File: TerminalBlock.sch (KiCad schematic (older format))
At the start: 0 parts

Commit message: Refactoring and Created key shortcuts
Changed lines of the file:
@@
 $Descr A4 11693 8268
 encoding utf-8
-Sheet 9 9
+Sheet 8 9
 Title ""
-Date "9 feb 2014"
+Date "18 feb 2014"
 Rev ""
 Comp ""
@@
 L +3.3V #PWR?
 U 1 1 52F86033
-P 2850 1050
-F 0 "#PWR?" H 2850 1010 30  0001 C CNN
-F 1 "+3.3V" H 2850 1160 30  0000 C CNN
-F 2 "" H 2850 1050 60  0000 C CNN
-F 3 "" H 2850 1050 60  0000 C CNN
-	1    2850 1050
+P 2100 850
+F 0 "#PWR?" H 2100 810 30  0001 C CNN
+F 1 "+3.3V" H 2100 960 30  0000 C CNN
+F 2 "" H 2100 850 60  0000 C CNN
+F 3 "" H 2100 850 60  0000 C CNN
+	1    2100 850
 	1    0    0    -1
 $EndComp
@@
 L +5V #PWR?
 U 1 1 52F86042
-P 2850 1400
-F 0 "#PWR?" H 2850 1490 20  0001 C CNN
-F 1 "+5V" H 2850 1490 30  0000 C CNN
-F 2 "" H 2850 1400 60  0000 C CNN
-F 3 "" H 2850 1400 60  0000 C CNN
-	1    2850 1400
+P 2100 1200
+F 0 "#PWR?" H 2100 1290 20  0001 C CNN
+F 1 "+5V" H 2100 1290 30  0000 C CNN
+F 2 "" H 2100 1200 60  0000 C CNN
+F 3 "" H 2100 1200 60  0000 C CNN
+	1    2100 1200
 	1    0    0    -1
 $EndComp
@@
 L GND #PWR?
 U 1 1 52F86051
-P 2850 1750
-F 0 "#PWR?" H 2850 1750 30  0001 C CNN
-F 1 "GND" H 2850 1680 30  0001 C CNN
-F 2 "" H 2850 1750 60  0000 C CNN
-F 3 "" H 2850 1750 60  0000 C CNN
-	1    2850 1750
+P 2100 1550
+F 0 "#PWR?" H 2100 1550 30  0001 C CNN
+F 1 "GND" H 2100 1480 30  0001 C CNN
+F 2 "" H 2100 1550 60  0000 C CNN
+F 3 "" H 2100 1550 60  0000 C CNN
+	1    2100 1550
 	1    0    0    -1
 $EndComp

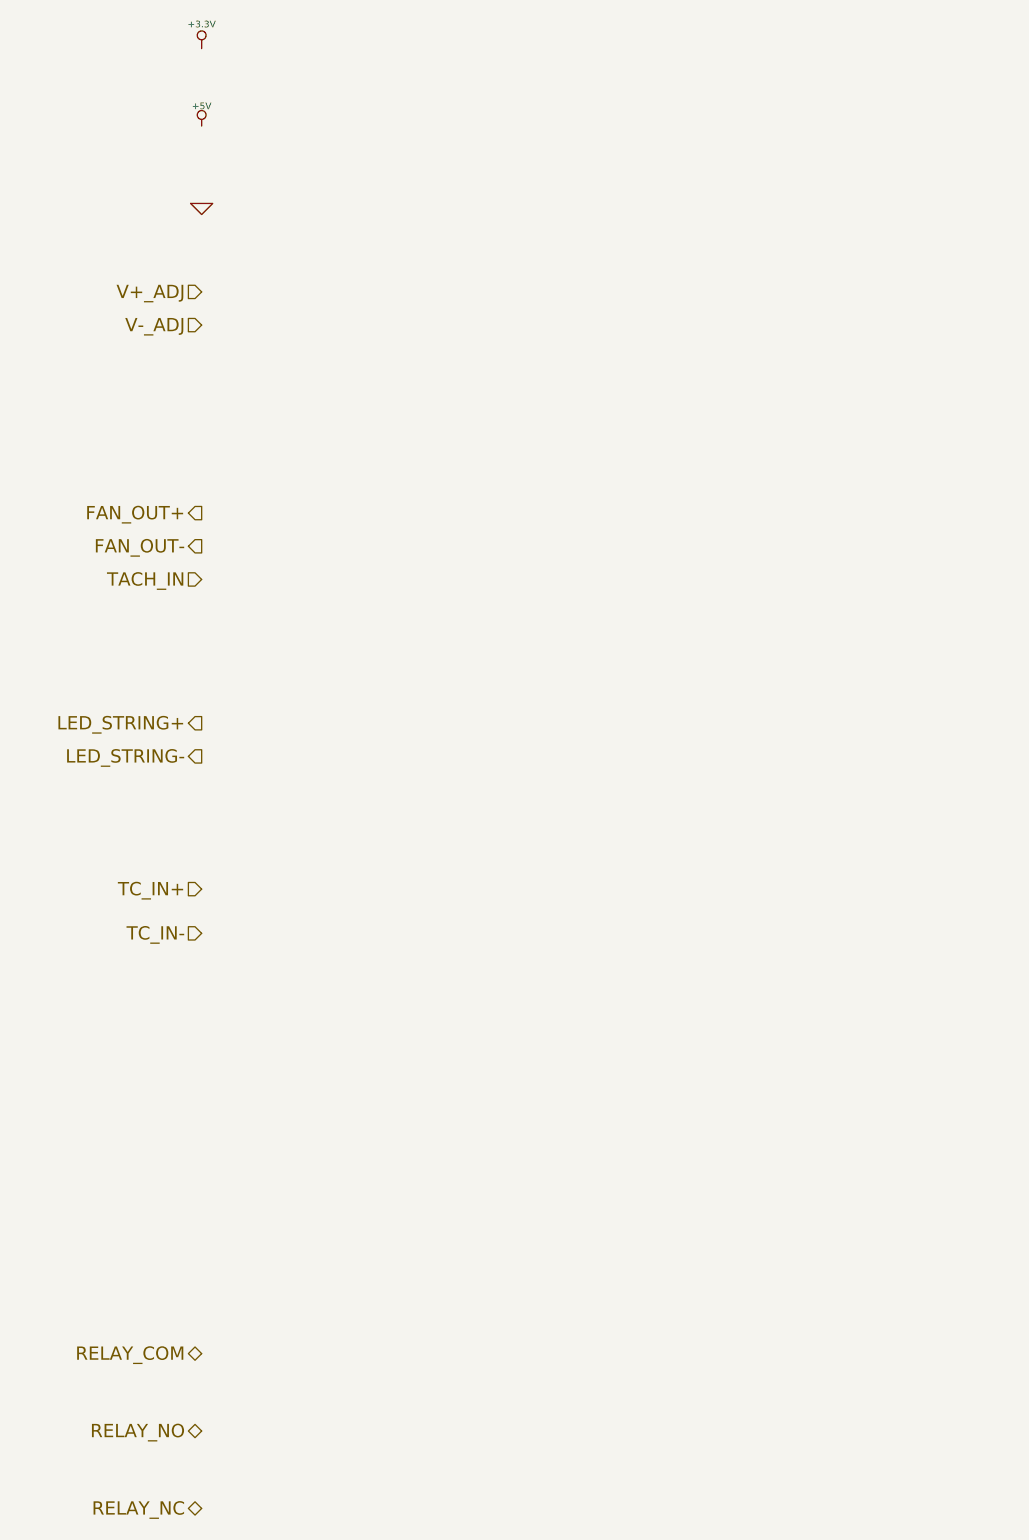
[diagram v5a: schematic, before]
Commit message: Terminal block and Arduino: assc/placement
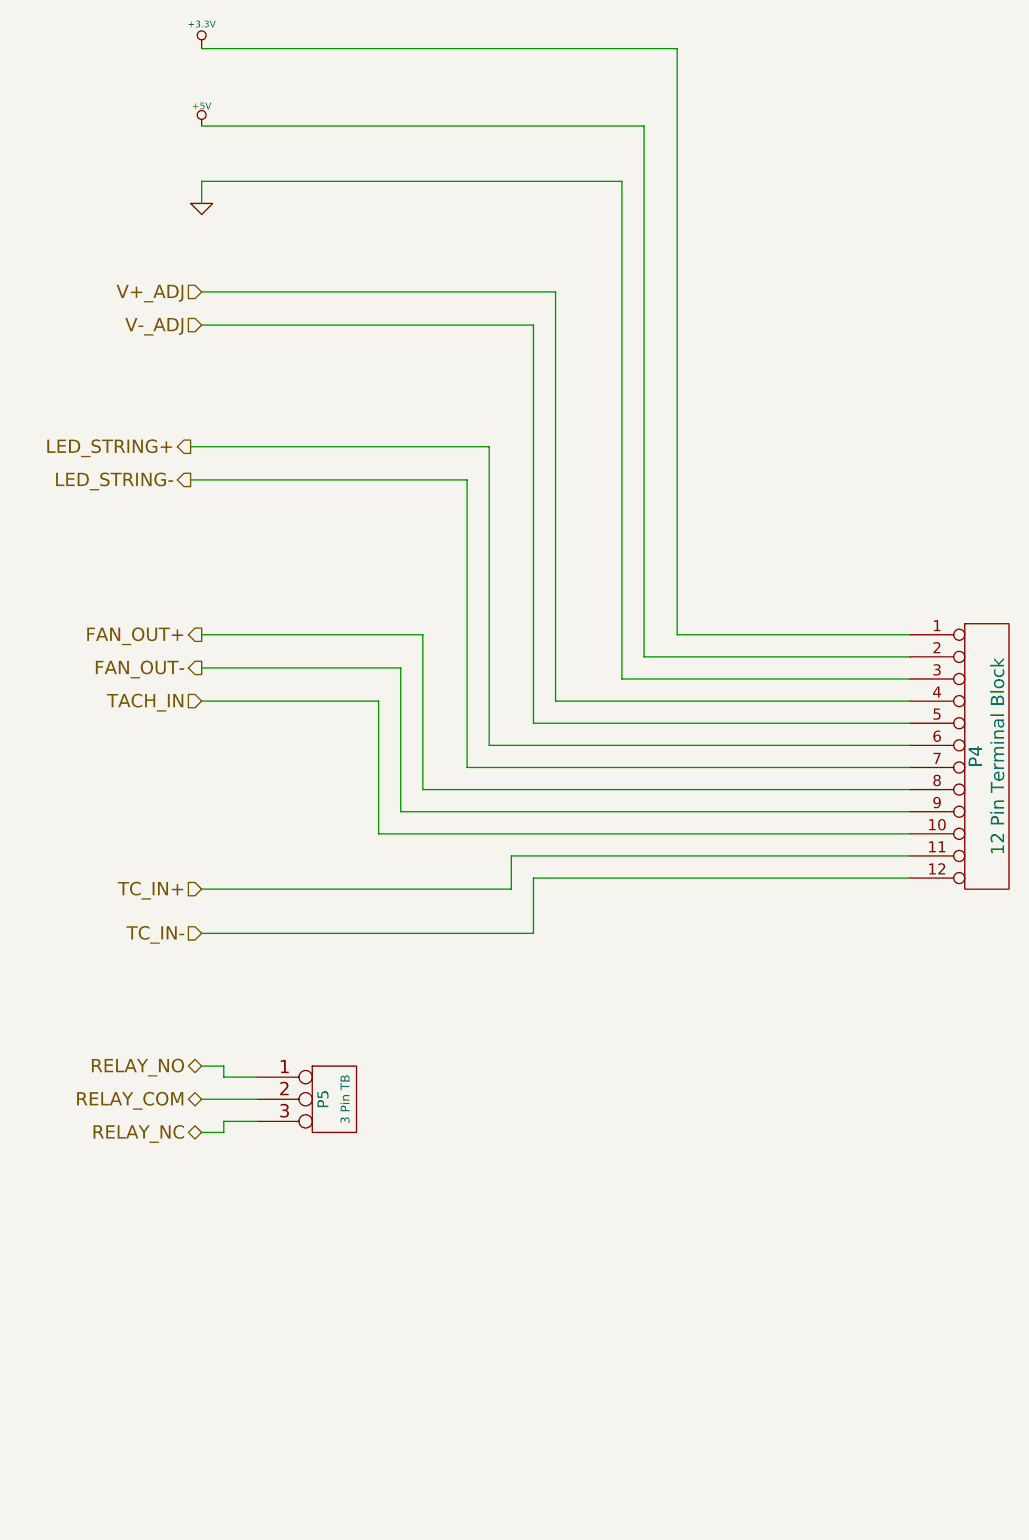
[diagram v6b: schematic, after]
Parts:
- added P4: 12 Pin Terminal Block, symbol CONN_12
- added P5: 3 Pin TB, symbol CONN_3
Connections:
- net +3.3V: now also P4.1 (P1)
- net +5V: now also P4.2 (P2)
- net FAN_OUT+: now also P4.8 (P8)
- net FAN_OUT-: now also P4.9 (P9)
- net GND: now also P4.3 (P3)
- net LED_STRING+: now also P4.6 (P6)
- net LED_STRING-: now also P4.7 (P7)
- net RELAY_COM: now also P5.2 (PM)
- net RELAY_NC: now also P5.3 (P3)
- net RELAY_NO: now also P5.1 (P1)
- net TACH_IN: now also P4.10 (P10)
- net TC_IN+: now also P4.11 (P11)
- net TC_IN-: now also P4.12 (P12)
- net V+_ADJ: now also P4.4 (P4)
- net V-_ADJ: now also P4.5 (P5)
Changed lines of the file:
@@
 $Descr A4 11693 8268
 encoding utf-8
-Sheet 8 9
+Sheet 6 9
 Title ""
-Date "21 feb 2014"
+Date "22 feb 2014"
 Rev ""
 Comp ""
@@
 Text HLabel 2100 2100 0    60   Input ~ 0
 V-_ADJ
-Text HLabel 2100 2950 0    60   Output ~ 0
+Text HLabel 2100 3500 0    60   Output ~ 0
 FAN_OUT+
-Text HLabel 2100 3100 0    60   Output ~ 0
+Text HLabel 2100 3650 0    60   Output ~ 0
 FAN_OUT-
-Text HLabel 2100 3250 0    60   Input ~ 0
+Text HLabel 2100 3800 0    60   Input ~ 0
 TACH_IN
-Text HLabel 2100 3900 0    60   Output ~ 0
+Text HLabel 2050 2650 0    60   Output ~ 0
 LED_STRING+
-Text HLabel 2100 4050 0    60   Output ~ 0
+Text HLabel 2050 2800 0    60   Output ~ 0
 LED_STRING-
 Text HLabel 2100 4650 0    60   Input ~ 0
@@
 Text HLabel 2100 4850 0    60   Input ~ 0
 TC_IN-
-Text HLabel 2100 6750 0    60   BiDi ~ 0
+Text HLabel 2100 5600 0    60   BiDi ~ 0
 RELAY_COM
-Text HLabel 2100 7100 0    60   BiDi ~ 0
+Text HLabel 2100 5450 0    60   BiDi ~ 0
 RELAY_NO
-Text HLabel 2100 7450 0    60   BiDi ~ 0
+Text HLabel 2100 5750 0    60   BiDi ~ 0
 RELAY_NC
 $Comp
@@
 	1    0    0    -1
 $EndComp
+$Comp
+L CONN_12 P4
+U 1 1 530818DD
+P 5650 4050
+F 0 "P4" V 5600 4050 60  0000 C CNN
+F 1 "12 Pin Terminal Block" V 5700 4050 60  0000 C CNN
+F 2 "" H 5650 4050 60  0000 C CNN
+F 3 "" H 5650 4050 60  0000 C CNN
+F 4 "On Shore" H 5650 4050 60  0001 C CNN "MFG Name"
+F 5 "OSTTE120104" H 5650 4050 60  0001 C CNN "MFG Part Number"
+	1    5650 4050
+	1    0    0    -1
+$EndComp
+$Comp
+L CONN_3 P5
+U 1 1 53081E5F
+P 2700 5600
+F 0 "P5" V 2650 5600 50  0000 C CNN
+F 1 "3 Pin TB" V 2750 5600 40  0000 C CNN
+F 2 "" H 2700 5600 60  0000 C CNN
+F 3 "" H 2700 5600 60  0000 C CNN
+F 4 "Phoenix" H 2700 5600 60  0001 C CNN "MFG Name"
+F 5 "1935174" H 2700 5600 60  0001 C CNN "MFG Part Number"
+	1    2700 5600
+	1    0    0    -1
+$EndComp
+Wire Wire Line
+	2100 850  4250 850
+Wire Wire Line
+	4250 850  4250 3500
+Wire Wire Line
+	4250 3500 5300 3500
+Wire Wire Line
+	2100 1200 4100 1200
+Wire Wire Line
+	4100 1200 4100 3600
+Wire Wire Line
+	4100 3600 5300 3600
+Wire Wire Line
+	2100 1550 2100 1450
+Wire Wire Line
+	2100 1450 4000 1450
+Wire Wire Line
+	4000 1450 4000 3700
+Wire Wire Line
+	4000 3700 5300 3700
+Wire Wire Line
+	2100 1950 3700 1950
+Wire Wire Line
+	3700 1950 3700 3800
+Wire Wire Line
+	3700 3800 5300 3800
+Wire Wire Line
+	2100 2100 3600 2100
+Wire Wire Line
+	3600 2100 3600 3900
+Wire Wire Line
+	3600 3900 5300 3900
+Wire Wire Line
+	2050 2650 3400 2650
+Wire Wire Line
+	3400 2650 3400 4000
+Wire Wire Line
+	3400 4000 5300 4000
+Wire Wire Line
+	5300 4100 3300 4100
+Wire Wire Line
+	3300 4100 3300 2800
+Wire Wire Line
+	3300 2800 2050 2800
+Wire Wire Line
+	2100 3500 3100 3500
+Wire Wire Line
+	3100 3500 3100 4200
+Wire Wire Line
+	3100 4200 5300 4200
+Wire Wire Line
+	5300 4300 3000 4300
+Wire Wire Line
+	3000 4300 3000 3650
+Wire Wire Line
+	3000 3650 2100 3650
+Wire Wire Line
+	2100 3800 2900 3800
+Wire Wire Line
+	2900 3800 2900 4400
+Wire Wire Line
+	2900 4400 5300 4400
+Wire Wire Line
+	5300 4500 3500 4500
+Wire Wire Line
+	3500 4500 3500 4650
+Wire Wire Line
+	3500 4650 2100 4650
+Wire Wire Line
+	2100 4850 3600 4850
+Wire Wire Line
+	3600 4850 3600 4600
+Wire Wire Line
+	3600 4600 5300 4600
+Wire Wire Line
+	2350 5600 2100 5600
+Wire Wire Line
+	2100 5450 2200 5450
+Wire Wire Line
+	2200 5450 2200 5500
+Wire Wire Line
+	2200 5500 2350 5500
+Wire Wire Line
+	2100 5750 2200 5750
+Wire Wire Line
+	2200 5750 2200 5700
+Wire Wire Line
+	2200 5700 2350 5700
 $EndSCHEMATC
